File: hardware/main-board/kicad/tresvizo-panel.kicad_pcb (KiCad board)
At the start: 4 copper layers, 82.8 x 79 mm, 135 parts, among them J101 PANEL_USB, J102 BATTERY, J301 GNSS, J401 TF-015, J402 BOTON, J403 OLED, J404 NTC, J405 IMU, J501 USB_C, J502 PANEL_USB, Q101 AO3400A, Q102 AO3401A, Q103 AO3400A, Q401 AO3401A, Q402 AO3400A, SW201 RESET, SW202 BOOT, U101 USBLC6-2SC6, U102 BQ25798RQMR, U103 MAX17048G+T10, U105 TPS62903RPJR, U201 ESP32-S3-WROOM-1-N16R2, U301 TPS63070RNMR, U302 USBLC6-2SC6, U303 USBLC6-2SC6, U501 USBLC6-2SC6

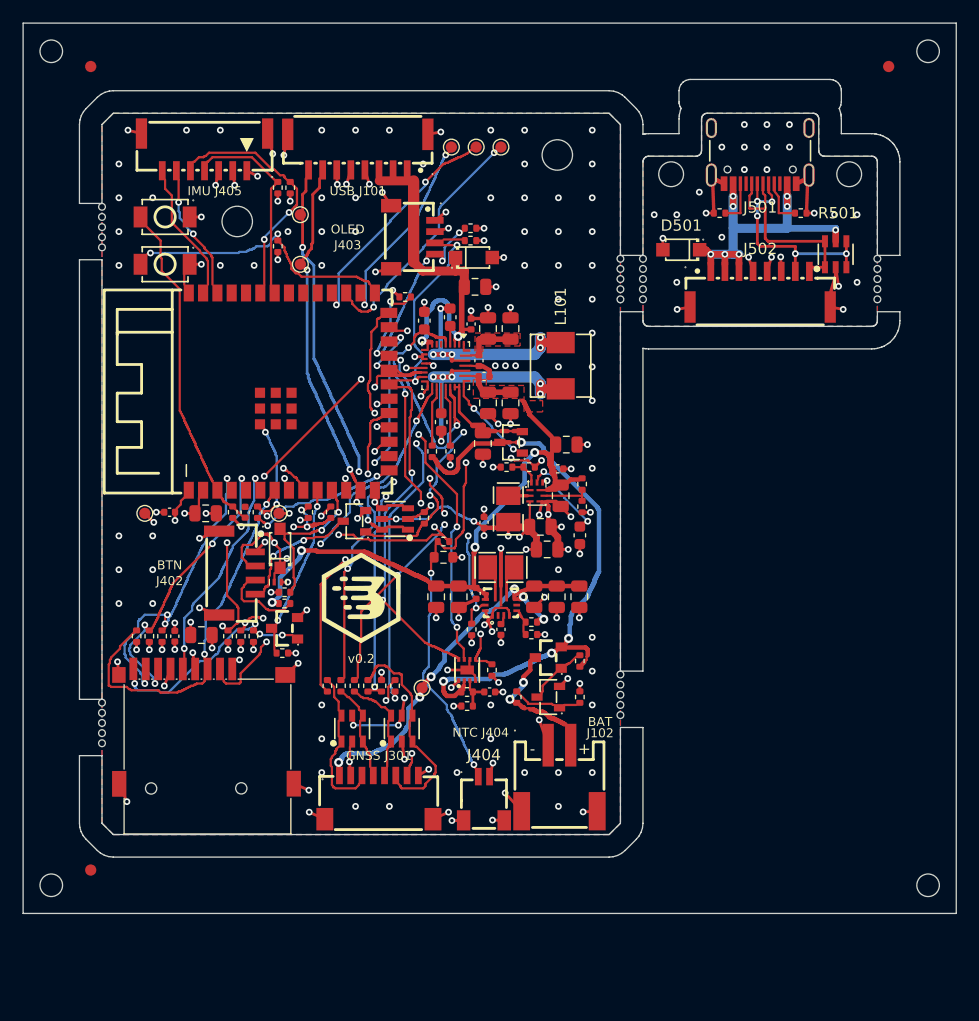
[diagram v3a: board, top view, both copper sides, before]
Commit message: Placa principal v0.3 compacta: 36 × 71.5 mm para el tubo de Ø52, con USB-C, OLED, botón, LED y BMI088 en la placa
- Rama exploratoria pedida por el propietario el 07-10-2026. Especificación, interfaces con la
  carcasa, colocación y auditoría en research/v03-compacta.md.
- Esquema (ERC 0):
  - USB-C TYPE-C-31-M-12 con Rd de 5.1k, TVS SMF15A y USBLC6;
  - pulsador TS-1187A a BTN_N;
  - LED de estado en GPIO48 con 330 Ω;
  - OLED del propietario soldada sobre pads SMD (J403);
  - BMI088 por I2C (GPIO41/42, INT1 en GPIO2 e INT3 en GPIO1);
  - J102 en GH 4, con dos contactos por polo;
  - TP208 y TP209 en la UART0.
  Fuera J402, J405 y Q402; la panel-usb ya no se usa.
- Placa de 4 capas con muescas para la funda del USB-C y para la clavija SMA de la carrier.
  - Los bloques del cargador y de los reguladores se mueven sin cambiar su geometría interna.
  - La antena del WROOM va hacia −X, con zona sin cobre.
  - Panel de una sola placa.
  - DRC con 0 violaciones, 0 sin conectar y 0 de paridad; el panel, igual.
- Auditoría eléctrica independiente (08-10-2026), con sus siete puntos corregidos:
  - las soldaduras de la OLED ya no quedan frente al SMA de la carrier;
  - puentes del panel lejos del IMU y de los condensadores de potencia;
  - zona sin cobre de la antena más grande;
  - GND de J102 y vías dobles en VPACK;
  - vías junto al pad de tierra del WROOM;
  - LED más brillante;
  - pads de la UART.
- cad/export_board_step.py exporta el STEP en los ejes de la carcasa, con los modelos de LCSC
  corregidos. cad/check_heights.py comprueba los altos contra el tubo: todas las piezas caben con
  0.3 mm de aire.
- Cambios en los scripts:
  - route_rest.py admite límites de búsqueda por entorno;
  - fanout.py respeta las vías prerruteadas;
  - finish_pcb.py --final quita las vías sin uso;
  - cost_jlc.py sirve para una sola placa.
- Costo estimado en JLCPCB: 236.43 USD por 5 placas montadas, sin el PCB ni el envío.
- El build casi siempre se repite igual. En una de cuatro corrid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
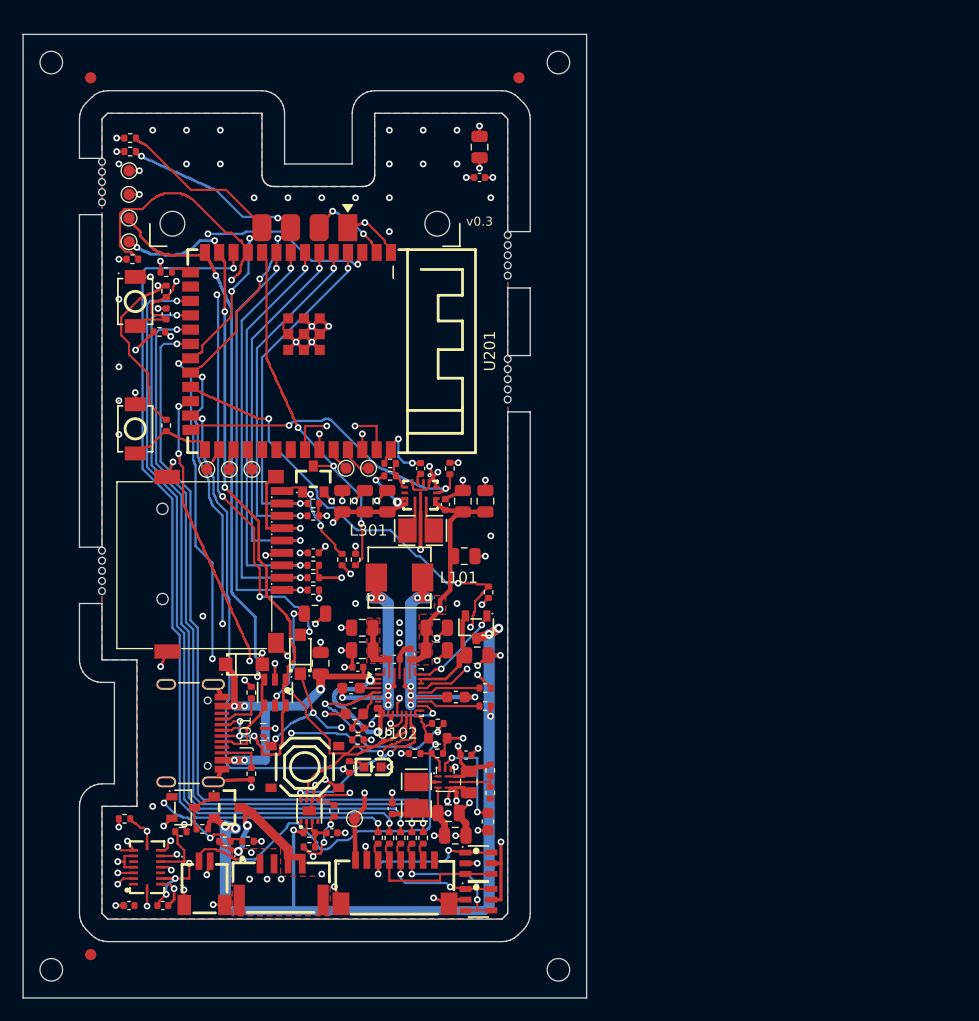
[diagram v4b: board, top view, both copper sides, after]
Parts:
- removed D501: SMF15A, tresvizo_lcsc:SOD-123FL_L2.7-W1.8-LS3.8-RD
- removed H1, H2: MountingHole_2.7mm, MountingHole_2.7mm
- removed H501, H502: MountingHole_2.2mm_M2, MountingHole_2.2mm_M2
- removed J402: BOTON, tresvizo_lcsc:CONN-SMD_4P-P1.25_SM04B-GHS-TB-LF-SN
- removed J405: IMU, tresvizo_lcsc:CONN-SMD_SM7B-GHS-TB-LF-SN
- removed J501: USB_C, tresvizo_lcsc:USB-C_SMD-TYPE-C-31-M-12
- removed J502: PANEL_USB, tresvizo_lcsc:CONN-SMD_8P-P1.25_XUNPU-WAFER-GH1.25-8PWB
- removed MB5: MB5, 
- removed MB6: MB6, 
- removed Q402: AO3400A, tresvizo_lcsc:SOT-23-3_L2.9-W1.3-P1.90-LS2.4-BR
- removed R410: 100k, Resistor_SMD:R_0402_1005Metric
- removed R501, R502: 5.1k, Resistor_SMD:R_0402_1005Metric
- removed U501: USBLC6-2SC6, tresvizo_lcsc:SOT-23-6_L2.9-W1.6-P0.95-LS2.8-BL
- added C403: 100nF, Capacitor_SMD:C_0402_1005Metric, F.Cu at (109.4, 177.3)
- added C404: 100nF, Capacitor_SMD:C_0402_1005Metric, F.Cu at (112.4, 177.3)
- added D403: KT-0603R, tresvizo_lcsc:LED-SMD_L1.6-W0.8-R-RD, F.Cu at (131.0, 165.0)
- added R119: 5.1k, Resistor_SMD:R_0402_1005Metric, F.Cu at (120.2, 158.4)
- added R120: 5.1k, Resistor_SMD:R_0402_1005Metric, F.Cu at (120.2, 165.6)
- added SW401: BOTON, tresvizo_lcsc:SW-SMD_4P-L5.1-W5.1-P3.70-LS6.5-TL_H1.5, F.Cu at (125.0, 165.0)
- added TP208: U0TXD, TestPoint:TestPoint_Pad_D1.0mm, F.Cu at (130.7, 138.5)
- added TP209: U0RXD, TestPoint:TestPoint_Pad_D1.0mm, F.Cu at (128.7, 138.5)
- added U401: BMI088, tresvizo_lcsc:LGA-16_L4.5-W3.0-P0.50-BL, F.Cu at (111.0, 173.9)
- J101: value PANEL_USB -> USB_C; footprint tresvizo_lcsc:CONN-SMD_8P-P1.25_XUNPU-WAFER-GH1.25-8PWB -> tresvizo_lcsc:USB-C_SMD-TYPE-C-31-M-12
- J102: footprint tresvizo_lcsc:CONN-SMD_P2.00_S2B-PH-SM4-TB-LF-SN -> tresvizo_lcsc:CONN-SMD_4P-P1.25_SM04B-GHS-TB-LF-SN
- J403: footprint tresvizo_lcsc:CONN-SMD_4P-P1.00_SM04B-SRSS-TB-LF-SN -> tresvizo_lcsc:OLED_0.96in_I2C_4P_P2.54mm
- R409: value 100 -> 330
- moved R412 57.9 mm to (109.0, 169.6), turned to 0 degrees
- moved R411 57.8 mm to (114.0, 170.8), turned to 0 degrees
- moved J101 53.6 mm to (115.2, 162.0), turned to -90 degrees
- moved D101 41.5 mm to (119.6, 155.9)
- moved C201 40.6 mm to (140.5, 110.0), turned to 90 degrees
- moved C202 40.5 mm to (140.5, 112.7)
- moved TP204 37.4 mm to (118.3, 138.6)
- moved R308 37.1 mm to (112.1, 126.4), turned to 180 degrees
- moved R109 36.7 mm to (115.9, 170.5), turned to 180 degrees
- moved C104 36.1 mm to (126.4, 155.8), turned to 90 degrees
- moved TP203 35.9 mm to (116.3, 138.6)
- moved C103 35.4 mm to (129.4, 160.3), turned to 180 degrees
- moved TP205 34.8 mm to (120.3, 138.6)
- moved C101 34.1 mm to (129.1, 158.0), turned to 180 degrees
- moved Q103 33.8 mm to (114.2, 168.6), turned to 180 degrees
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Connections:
- net /microSD, IMU por conector y panel/SD_CD_N renamed /microSD, IMU, OLED, botón y LED/SD_CD_N
- J102 pad 2: /Alimentación, carga y batería/VBATT_IN -> GND
- J403 pad 3: I2C_SDA -> I2C_SCL
- J403 pad 4: I2C_SCL -> I2C_SDA
- R409 pad 1: VSYS -> LED_STATUS
- R409 pad 2: /microSD, IMU por conector y panel/BTN_LED_A -> /microSD, IMU, OLED, botón y LED/LED_STATUS_A
- U201 pad 25: BTN_LED_EN -> LED_STATUS
- U201 pad 36: unconnected-(U201-RXD0-Pad36) -> /ESP32-S3/ESP_RXD0
- U201 pad 37: unconnected-(U201-TXD0-Pad37) -> /ESP32-S3/ESP_TXD0
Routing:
- net GNSS_TX_MCU: track 20.1 -> 77.2 mm
- net IMU_INT1: track 10.5 -> 63.1 mm
- net IMU_INT3: track 10.9 -> 59.1 mm, vias 0 -> 2
- net BTN_SENSE_N: track 12.3 -> 57.6 mm, vias 2 -> 5
- net GNSS_TXD2_MCU: track 24.5 -> 69.4 mm, vias 3 -> 2
- net I2C_SDA: track 50.6 -> 93.7 mm, vias 4 -> 8
- net LED_STATUS: track 0.00 -> 43.0 mm, vias 0 -> 2
- net GNSS_EVENT_MCU: track 26.8 -> 69.1 mm
- net GNSS_PPS_MCU: track 29.0 -> 68.5 mm, vias 5 -> 2
- net IMU_SDA: track 16.1 -> 55.1 mm, vias 0 -> 3
- net +3V3: track 48.9 -> 87.5 mm, vias 35 -> 34
- net I2C_SCL: track 55.0 -> 92.0 mm, vias 8 -> 7
- net GNSS_RESET_MCU: track 30.1 -> 66.6 mm, vias 3 -> 2
- net IMU_SCL: track 20.0 -> 52.1 mm
- net PUSB/VBUS: track 29.8 -> 0.00 mm, vias 8 -> 0
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- removed copper zone on B.Cu, net PUSB/GND
- removed copper zone on F.Cu, net PUSB/GND
- removed copper zone on In1.Cu, net PUSB/GND
- removed copper zone on In2.Cu, net PUSB/GND
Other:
- board size 82.8 x 79 mm -> 50 x 85.5 mm
- board text added: "1-2 BAT- 3-4 BAT+"
- board text added: "2S: R103=8.2k R116=3.9k U103=MAX17049"
- board text added: "2S: R112 NC R114 0R"
- board text added: "BAT J102"
- board text added: "TresVizo MeridianV - placa principal v0.3"
- board text added: "v0.3"
- board text removed: "+"
- board text removed: "-"
- board text removed: "2S: R103=8.2k R116=3.9k U103=MAX17049 R112 NC R114 0R"
- board text removed: "7 D- 8 D+ cable 1:1"
- board text removed: "BAT"
- board text removed: "BTN"
- board text removed: "IMU J405"
- board text removed: "J102"
- board text removed: "J402"
- board text removed: "J403"
- board text removed: "J502: 1-3 VBUS 4-6 GND"
- board text removed: "OLED"
- board text removed: "TresVizo MeridianV - placa principal v0.2"
- board text removed: "TresVizo USB-C panel v0.1"
- board text removed: "USB J101"
- board text removed: "v0.2"

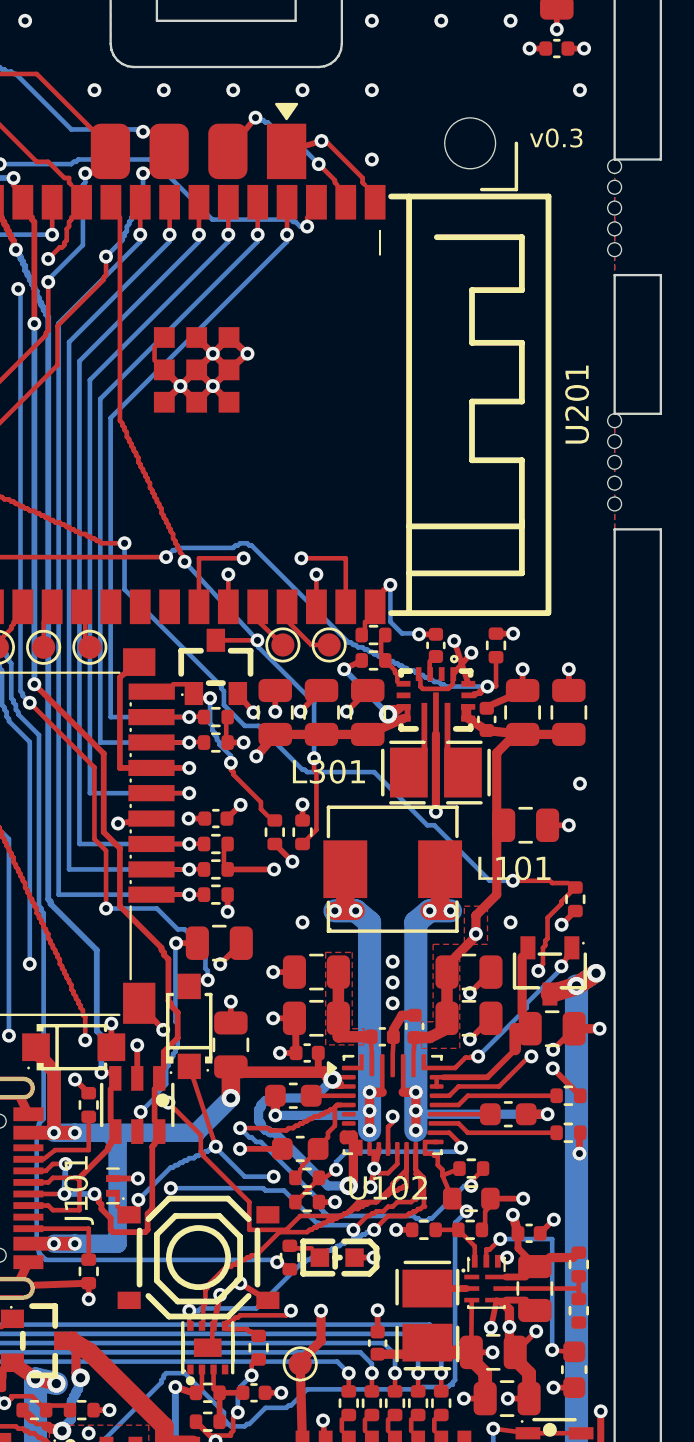
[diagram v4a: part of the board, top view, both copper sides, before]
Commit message: v0.3: endurecimiento de la placa y de la carcasa V3.0 (Ø56 × 111)
Carcasa V3.0:
- Tubo de Ø56 × 111 con pared de 2.4 (antes Ø52 × 100). Holguras, en la posición final y en los
  11 barridos de montaje:
  - 0.4 mm en los ajustes entre piezas impresas;
  - 0.25 por cara en los rieles de la placa;
  - 0.5 de aire a todo lo comprado.
  El coaxial va con curvas de R 10. La placa no cambió de sitio; la carrier va 0.1 más atrás.
- Antena:
  - SMA hembra de panel al centro de la tapa para la HA-901A. La tienda da conector macho
    («SMA-J»); si resulta hembra, un parámetro cambia la tapa a un paso de 12 mm.
  - Coaxial RG 178 B/U de unos 75 mm, con SMA macho acodado en la carrier.
  - Arandelas ISO 7092 en los tornillos de la antena.
- Correcciones de la revisión externa:
  - eje real de la tarjeta microSD (z 40.9), tomado de J401 y no de la ranura;
  - arnés real de la batería y la NTC, con su recorrido;
  - procedimiento de desarmado completo.
- Tapa de TPU amarrada para el USB-C y la microSD, logo en relieve de 0.5 al frente y líneas
  verticales decorativas atrás, como en V2.3.
- check_v3_0.py: 0 choques y guarda de pared sin faltantes. Se cumplen los objetivos de holgura; la
  pared más delgada mide 1.198 mm, en una unión.

Placa v0.3, sin mover piezas:
- C104, C106 y C107 pasan de 22 a 10 µF (C15850). La carga que pide el USB al enchufar baja de unos
  259 a 118 µC. Sigue arriba de la regla de 10 µF de USB 2.0: queda como decisión del propietario.
- VSYS por In2.Cu a 1.2 mm y GNSS_5V a 0.6 mm, con más vías.
- Tabla de valores para el firmware: ICHG de 1.5 A como máximo, límite de entrada, reinicio con el
  botón, OLED girada 180° y ejes del IMU.
- ERC 0. DRC 0/0/0 y panel 0/0. Dos builds iguales byte a byte. 234.15 USD por 5 placas montadas.
- check_heights.py lee el tubo de la carcasa y mide 0.5 de aire en radio: todas las piezas caben.

Pendiente: confirmar el conector de la antena, medir la carrier y la OLED, y el orden de los pines
de la OLED.
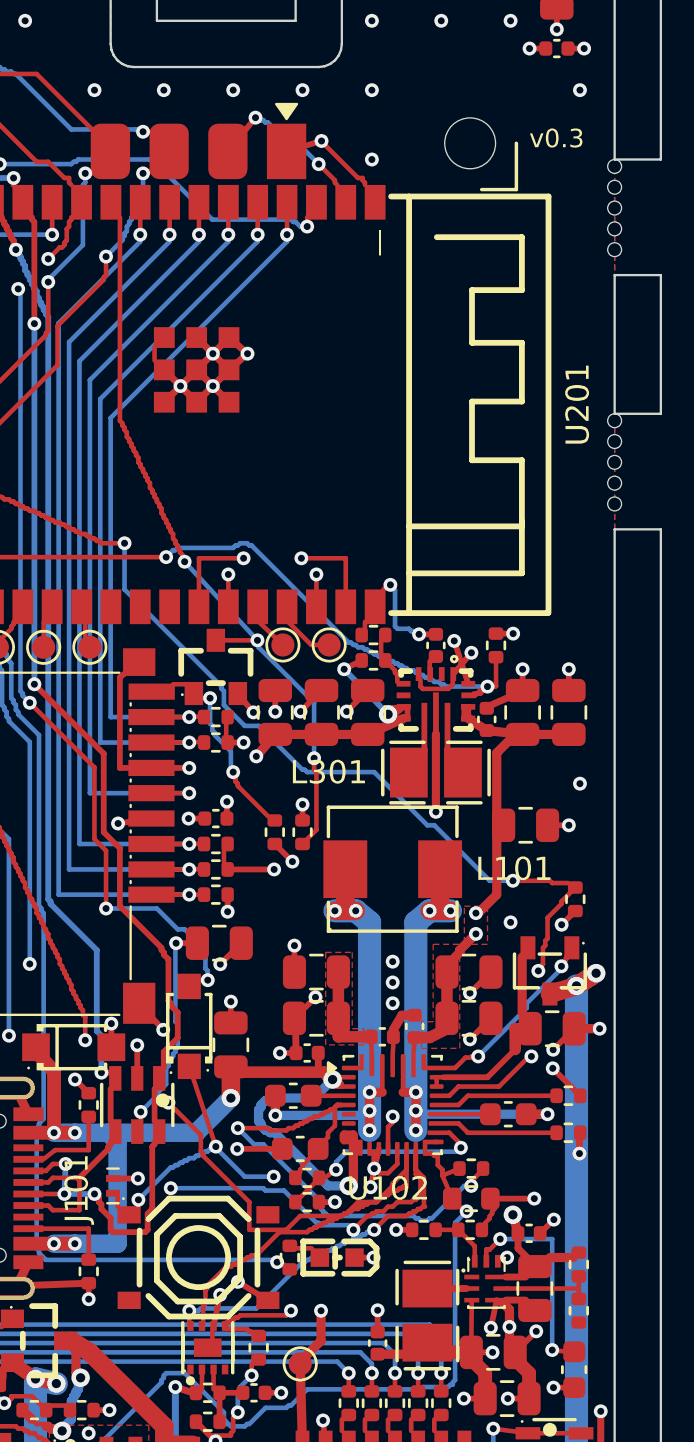
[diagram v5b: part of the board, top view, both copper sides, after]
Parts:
- removed the FID3 at (106.0, 181.7)
- removed the MB1 at (107.0, 111.3)
- added MB4: MB4, , F.Cu at (143.0, 128.8)
- added TH1: TH1, , F.Cu at (102.5, 102.5)
- C104, C106, C107: value 22uF -> 10uF
- FID3: renamed from TH1; value TH1 -> Fiducial_1mm_Mask2mm; footprint (none) -> Fiducial_1mm_Mask2mm
- MB1: renamed from MB2; value MB2 -> MB1
- MB2: renamed from MB3; value MB3 -> MB2
- MB3: renamed from MB4; value MB4 -> MB3
- moved FID3 79.2 mm to (106.0, 181.7)
- moved MB2 45.6 mm to (107.0, 145.8)
- moved MB1 34.5 mm to (107.0, 111.3)
- moved MB3 11.0 mm to (143.0, 117.8)
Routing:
- net GND: track 133.0 -> 134.6 mm, vias 112 -> 111
- net VSYS: track 36.5 -> 36.6 mm, vias 2 -> 3
